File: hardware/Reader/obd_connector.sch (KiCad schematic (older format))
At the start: 3 parts, among them CN1 AHDF15A-KG-TAXB

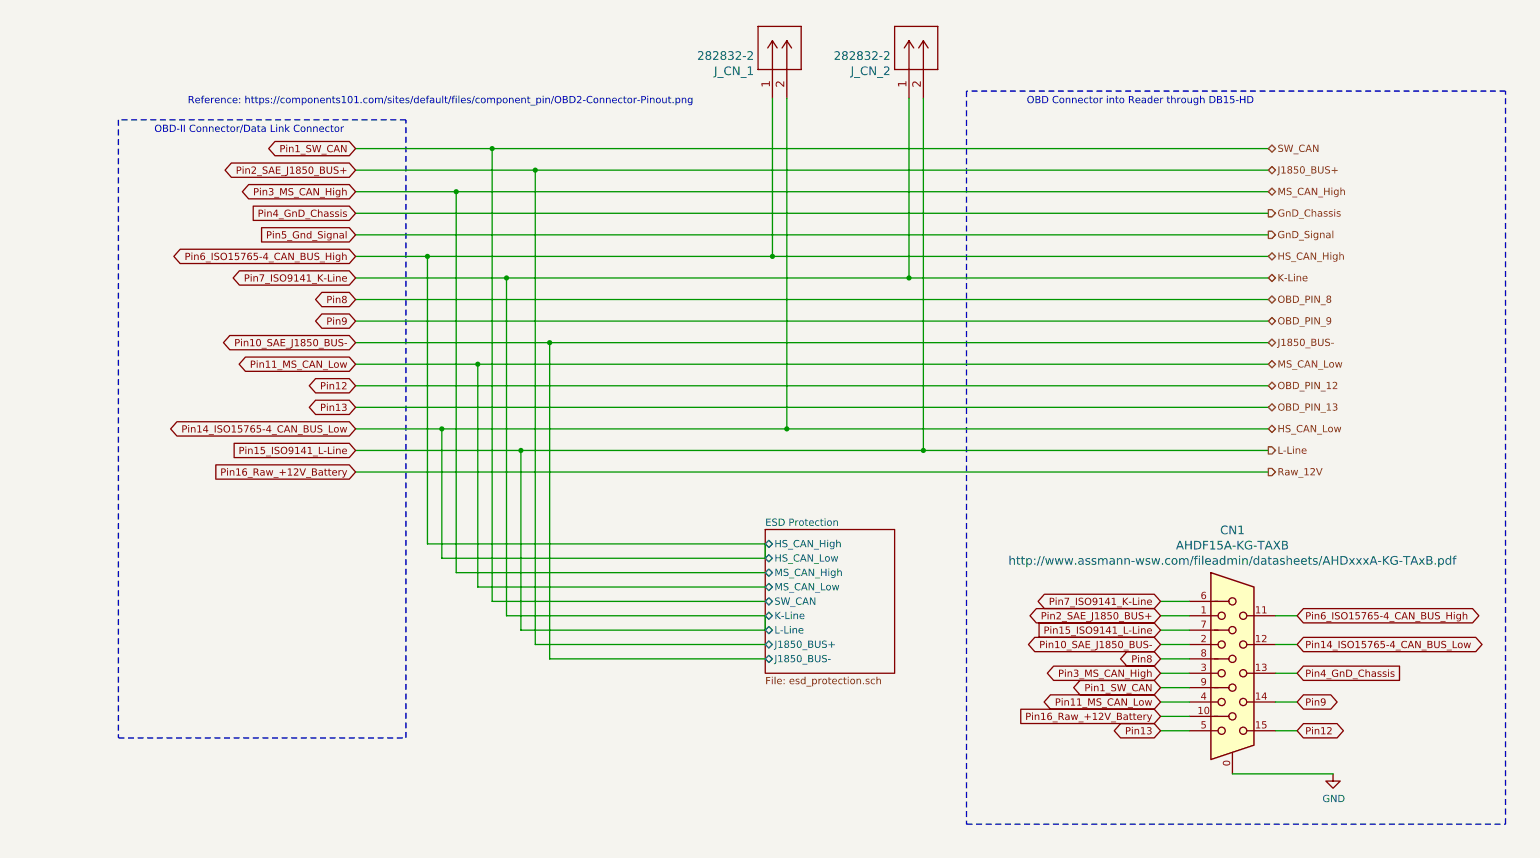
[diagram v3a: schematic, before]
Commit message: Fixed wiring issue on ESD Protection
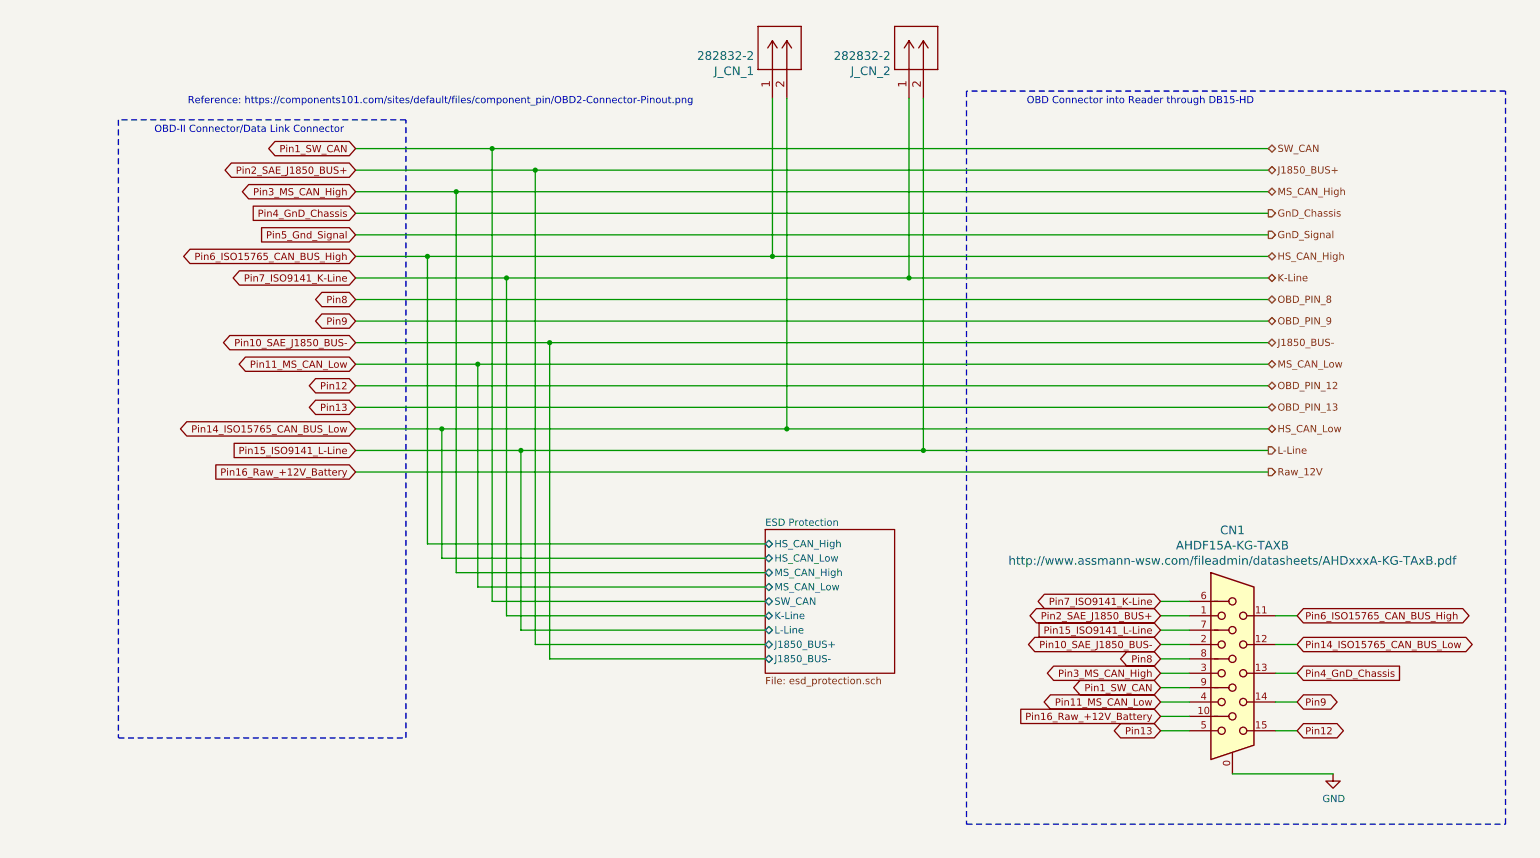
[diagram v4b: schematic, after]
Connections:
- net Pin15_ISO9141_L-Line: no longer CN1.6, J_CN_2.1
- net Pin14_ISO15765-4_CAN_BUS_Low renamed Pin14_ISO15765_CAN_BUS_Low
- net Pin14_ISO15765_CAN_BUS_Low: no longer CN1.11, J_CN_1.1
- new net Pin6_ISO15765_CAN_BUS_High: CN1.11, J_CN_1.1
- new net Pin7_ISO9141_K-Line: CN1.6, J_CN_2.1

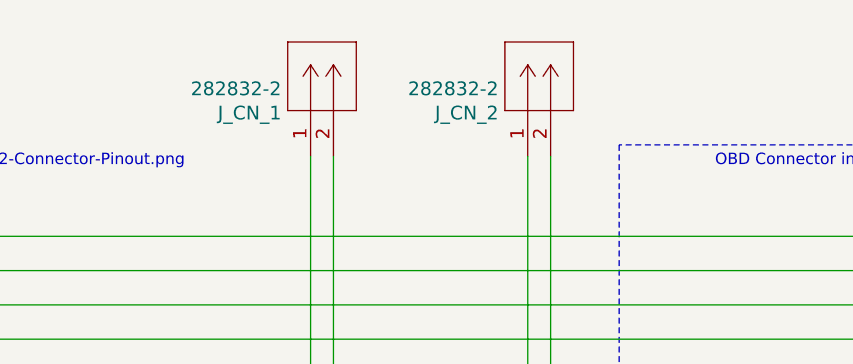
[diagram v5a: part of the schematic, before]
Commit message: Fixed bugs in schematic. Updated BOM list. Swapped to using ESP32 holder. Updated PCB layout to v0.0.2. Updated schematic to v0.0.4
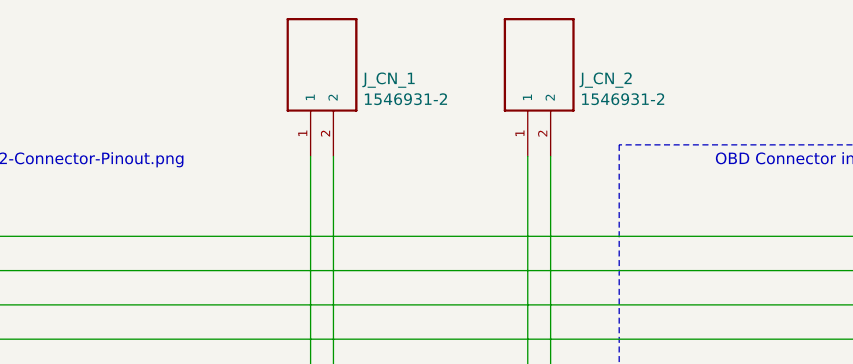
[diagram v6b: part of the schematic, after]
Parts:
- removed J_CN_1, J_CN_2: 282832-2, footprints:282832-2, symbol 2828322:282832-2
- added J_CN_1, J_CN_2: 1546931-2, footprints:1546931-2, symbol 1546931-2:1546931-2
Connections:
- net Pin14_ISO15765_CAN_BUS_Low: now also J_CN_1.2
- net Pin15_ISO9141_L-Line: now also J_CN_2.2
- net Pin6_ISO15765_CAN_BUS_High: now also J_CN_1.1
- net Pin7_ISO9141_K-Line: now also J_CN_2.1
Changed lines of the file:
@@
 Sheet 11 19
 Title "CANnect Reader | OBD Connector"
-Date "2020-10-27"
-Rev "0.0.03"
+Date "2020-10-28"
+Rev "0.0.04"
 Comp "CANtech"
 Comment1 "Created by Choong Jin Ng | jin8383@gmail.com"
@@
 	5150 2300 8600 2300
 Wire Wire Line
-	6200 1200 6200 3650
-Connection ~ 6200 3650
-Wire Wire Line
-	6200 3650 8600 3650
-Wire Wire Line
 	2750 2300 2750 4300
 Wire Wire Line
@@
 Wire Wire Line
 	3600 2900 8600 2900
-Wire Wire Line
-	3400 3650 6200 3650
 Wire Notes Line
 	10250 6250 10250 1150
@@
 Text GLabel 7850 4700 0    50   BiDi ~ 0
 Pin7_ISO9141_K-Line
-$Comp
-L 2828322:282832-2 J_CN_2
-U 1 1 5F984F05
-P 6100 1200
-F 0 "J_CN_2" V 6289 1328 60  0000 L CNN
-F 1 "282832-2" V 6395 1328 60  0000 L CNN
-F 2 "footprints:282832-2" H 6500 1140 60  0001 C CNN
-F 3 "https://www.te.com/commerce/DocumentDelivery/DDEController?Action=srchrtrv&DocNm=282832&DocType=Customer+Drawing&DocLang=English" V 6395 1328 60  0001 L CNN
-F 4 "282832-2" H 6100 1200 50  0001 C CNN "Part Name"
-F 5 "DigiKey Canada" H 6100 1200 50  0001 C CNN "Vendor"
-F 6 "TE Connectivity AMP Connectors" H 6100 1200 50  0001 C CNN "Manufacturer"
-F 7 "A113314-ND" H 6100 1200 50  0001 C CNN "digikeypn"
-	1    6100 1200
-	0    -1   -1   0
-$EndComp
 Wire Wire Line
 	5150 1200 5150 2300
-Wire Wire Line
-	3300 2450 6100 2450
-Wire Wire Line
-	6100 2450 8600 2450
-Connection ~ 6100 2450
-Wire Wire Line
-	6100 1200 6100 2450
 Wire Wire Line
 	2850 3500 5250 3500
@@
 Wire Wire Line
 	5250 1200 5250 3500
-$Comp
-L 2828322:282832-2 J_CN_1
-U 1 1 5F9847E5
-P 5150 1200
-F 0 "J_CN_1" V 5339 1328 60  0000 L CNN
-F 1 "282832-2" V 5445 1328 60  0000 L CNN
-F 2 "footprints:282832-2" H 5550 1140 60  0001 C CNN
-F 3 "https://www.te.com/commerce/DocumentDelivery/DDEController?Action=srchrtrv&DocNm=282832&DocType=Customer+Drawing&DocLang=English" V 5445 1328 60  0001 L CNN
-F 4 "282832-2" H 5150 1200 50  0001 C CNN "Part Name"
-F 5 "DigiKey Canada" H 5150 1200 50  0001 C CNN "Vendor"
-F 6 "TE Connectivity AMP Connectors" H 5150 1200 50  0001 C CNN "Manufacturer"
-F 7 "A113314-ND" H 5150 1200 50  0001 C CNN "digikeypn"
-	1    5150 1200
-	0    -1   -1   0
-$EndComp
 Wire Wire Line
 	2750 4300 5100 4300
@@
 F10 "J1850_BUS-" B L 5100 5100 50
 $EndSheet
+$Comp
+L 1546931-2:1546931-2 J_CN_1
+U 1 1 5FA0571B
+P 5250 800
+F 0 "J_CN_1" V 5189 670 50  0000 R CNN
+F 1 "1546931-2" V 5098 670 50  0000 R CNN
+F 2 "footprints:1546931-2" H 5250 800 50  0001 L BNN
+F 3 "https://www.te.com/commerce/DocumentDelivery/DDEController?Action=srchrtrv&DocNm=1-1773458-1_EURO_STYLE_QRG&DocType=DS&DocLang=English" H 5250 800 50  0001 L BNN
+F 4 "1546931-2" H 5250 800 50  0001 C CNN "Part Name"
+F 5 "TE Connectivity AMP Connectors" H 5250 800 50  0001 C CNN "Manufacturer"
+F 6 "Digikey Canada" H 5250 800 50  0001 C CNN "Vendor"
+F 7 "A97965-ND" H 5250 800 50  0001 C CNN "digikeypn"
+	1    5250 800
+	0    -1   -1   0
+$EndComp
+Connection ~ 6100 2450
+Wire Wire Line
+	6100 2450 8600 2450
+Wire Wire Line
+	3300 2450 6100 2450
+Wire Wire Line
+	3400 3650 6200 3650
+Wire Wire Line
+	6200 3650 8600 3650
+Connection ~ 6200 3650
+Wire Wire Line
+	6100 1200 6100 2450
+Wire Wire Line
+	6200 1200 6200 3650
+$Comp
+L 1546931-2:1546931-2 J_CN_2
+U 1 1 5FA083B3
+P 6200 800
+F 0 "J_CN_2" V 6139 670 50  0000 R CNN
+F 1 "1546931-2" V 6048 670 50  0000 R CNN
+F 2 "footprints:1546931-2" H 6200 800 50  0001 L BNN
+F 3 "https://www.te.com/commerce/DocumentDelivery/DDEController?Action=srchrtrv&DocNm=1-1773458-1_EURO_STYLE_QRG&DocType=DS&DocLang=English" H 6200 800 50  0001 L BNN
+F 4 "1546931-2" H 6200 800 50  0001 C CNN "Part Name"
+F 5 "TE Connectivity AMP Connectors" H 6200 800 50  0001 C CNN "Manufacturer"
+F 6 "Digikey Canada" H 6200 800 50  0001 C CNN "Vendor"
+F 7 "A97965-ND" H 6200 800 50  0001 C CNN "digikeypn"
+	1    6200 800
+	0    -1   -1   0
+$EndComp
 $EndSCHEMATC

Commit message: Revising reader
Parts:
- removed J_CN_1, J_CN_2: 1546931-2, footprints:1546931-2, symbol 1546931-2:1546931-2
- added J_CN_1: 4157, Connector_PinSocket_2.54mm:PinSocket_1x20_P2.54mm_Vertical, symbol CANtech:4157
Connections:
- net Pin10_SAE_J1850_BUS-: now also J_CN_1.12 (Pin_12)
- net Pin11_MS_CAN_Low: now also J_CN_1.17 (Pin_17)
- net Pin12: now also J_CN_1.10 (Pin_10)
- net Pin13: now also J_CN_1.11 (Pin_11)
- net Pin14_ISO15765_CAN_BUS_Low: now also J_CN_1.19 (Pin_19)
- net Pin15_ISO9141_L-Line: now also J_CN_1.14 (Pin_14)
- net Pin16_Raw_+12V_Battery: now also J_CN_1.9 (Pin_9)
- net Pin1_SW_CAN: now also J_CN_1.16 (Pin_16)
- net Pin2_SAE_J1850_BUS+: now also J_CN_1.13 (Pin_13)
- net Pin3_MS_CAN_High: now also J_CN_1.18 (Pin_18)
- net Pin4_GnD_Chassis: now also J_CN_1.5 (Pin_5)
- net Pin5_Gnd_Signal: now also J_CN_1.6 (Pin_6)
- net Pin6_ISO15765_CAN_BUS_High: now also J_CN_1.20 (Pin_20)
- net Pin7_ISO9141_K-Line: now also J_CN_1.15 (Pin_15)
- net Pin8: now also J_CN_1.7 (Pin_7)
- net Pin9: now also J_CN_1.8 (Pin_8)
- no-connect marks 0 -> 4
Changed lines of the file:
@@
 Sheet 11 19
 Title "CANnect Reader | OBD Connector"
-Date "2020-10-28"
-Rev "0.0.04"
+Date "2020-11-19"
+Rev "0.0.05"
 Comp "CANtech"
 Comment1 "Created by Choong Jin Ng | jin8383@gmail.com"
@@
 Wire Notes Line
 	10250 1150 6500 1150
-Connection ~ 5150 2300
-Wire Wire Line
-	5150 2300 8600 2300
 Wire Wire Line
 	2750 2300 2750 4300
 Wire Wire Line
-	2750 2300 5150 2300
-Wire Wire Line
 	2850 3500 2850 4400
 Wire Wire Line
@@
 	2950 1850 8600 1850
 Wire Wire Line
-	3100 3050 3100 4600
-Connection ~ 3100 3050
-Wire Wire Line
-	3100 3050 8600 3050
-Wire Wire Line
-	3200 4700 3200 1550
-Wire Wire Line
-	3200 1550 8600 1550
-Wire Wire Line
-	3300 4800 3300 2450
-Wire Wire Line
-	3400 4900 3400 3650
-Wire Wire Line
-	3500 5000 3500 1700
-Wire Wire Line
-	3500 1700 8600 1700
-Wire Wire Line
-	3600 2900 3600 5100
-Wire Wire Line
-	3600 2900 8600 2900
+	3250 4800 3250 2450
 Wire Notes Line
 	10250 6250 10250 1150
-Wire Wire Line
-	2250 3050 3100 3050
 Connection ~ 2850 3500
-Connection ~ 3400 3650
-Connection ~ 3600 2900
-Connection ~ 3300 2450
 Connection ~ 2750 2300
 Connection ~ 2950 1850
-Connection ~ 3500 1700
-Connection ~ 3200 1550
-Wire Wire Line
-	2250 3200 8600 3200
-Wire Wire Line
-	2250 2900 3600 2900
-Wire Wire Line
-	2250 2750 8600 2750
-Wire Wire Line
-	2250 2000 8600 2000
+Wire Wire Line
+	2250 2900 3550 2900
+Wire Wire Line
+	2250 2000 4250 2000
 Wire Wire Line
 	2250 1850 2950 1850
-Wire Wire Line
-	2250 1700 3500 1700
-Wire Wire Line
-	2250 1550 3200 1550
 Text GLabel 2250 2600 0    50   BiDi ~ 0
 Pin8
@@
 Pin9
 Wire Wire Line
-	2250 2150 8600 2150
+	2250 2150 4150 2150
 Wire Wire Line
 	2250 2300 2750 2300
 Wire Wire Line
-	2250 2600 8600 2600
-Wire Wire Line
-	2250 2450 3300 2450
-Wire Wire Line
-	2250 3350 8600 3350
+	2250 2600 4050 2600
+Wire Wire Line
+	2250 2450 3250 2450
+Wire Wire Line
+	2250 3350 3650 3350
 Wire Wire Line
 	2250 3500 2850 3500
-Wire Wire Line
-	2250 3800 8600 3800
-Wire Wire Line
-	2250 3650 3400 3650
 Text GLabel 2250 3650 0    50   Input ~ 0
 Pin15_ISO9141_L-Line
@@
 Pin7_ISO9141_K-Line
 Wire Wire Line
-	5150 1200 5150 2300
-Wire Wire Line
-	2850 3500 5250 3500
-Wire Wire Line
-	5250 3500 8600 3500
-Connection ~ 5250 3500
-Wire Wire Line
-	5250 1200 5250 3500
-Wire Wire Line
 	2750 4300 5100 4300
 Wire Wire Line
@@
 Wire Wire Line
 	2950 4500 5100 4500
-Wire Wire Line
-	3100 4600 5100 4600
-Wire Wire Line
-	5100 4700 3200 4700
-Wire Wire Line
-	5100 4800 3300 4800
-Wire Wire Line
-	5100 4900 3400 4900
-Wire Wire Line
-	5100 5000 3500 5000
-Wire Wire Line
-	3600 5100 5100 5100
 $Sheet
 S 5100 4200 900  1000
@@
 $EndSheet
 $Comp
-L 1546931-2:1546931-2 J_CN_1
-U 1 1 5FA0571B
-P 5250 800
-F 0 "J_CN_1" V 5189 670 50  0000 R CNN
-F 1 "1546931-2" V 5098 670 50  0000 R CNN
-F 2 "footprints:1546931-2" H 5250 800 50  0001 L BNN
-F 3 "https://www.te.com/commerce/DocumentDelivery/DDEController?Action=srchrtrv&DocNm=1-1773458-1_EURO_STYLE_QRG&DocType=DS&DocLang=English" H 5250 800 50  0001 L BNN
-F 4 "1546931-2" H 5250 800 50  0001 C CNN "Part Name"
-F 5 "TE Connectivity AMP Connectors" H 5250 800 50  0001 C CNN "Manufacturer"
-F 6 "Digikey Canada" H 5250 800 50  0001 C CNN "Vendor"
-F 7 "A97965-ND" H 5250 800 50  0001 C CNN "digikeypn"
-	1    5250 800
-	0    -1   -1   0
+L CANtech:4157 J_CN_1
+U 1 1 5FBE1A85
+P 4250 5850
+F 0 "J_CN_1" V 4663 5304 50  0000 C CNN
+F 1 "4157" V 4754 5304 50  0000 C CNN
+F 2 "Connector_PinSocket_2.54mm:PinSocket_1x20_P2.54mm_Vertical" H 4250 5850 50  0001 C CNN
+F 3 "https://media.digikey.com/pdf/Data%20Sheets/Adafruit%20PDFs/4157_Web.pdf" H 4250 5850 50  0001 C CNN
+F 4 "DigiKey Canada" H 4250 5850 50  0001 C CNN "Vendor"
+F 5 "Adafruit Industries LLC" H 4250 5850 50  0001 C CNN "Manufacturer"
+F 6 "1528-2929-ND" H 4250 5850 50  0001 C CNN "digikeypn"
+	1    4250 5850
+	0    1    1    0
 $EndComp
-Connection ~ 6100 2450
-Wire Wire Line
-	6100 2450 8600 2450
-Wire Wire Line
-	3300 2450 6100 2450
-Wire Wire Line
-	3400 3650 6200 3650
-Wire Wire Line
-	6200 3650 8600 3650
-Connection ~ 6200 3650
-Wire Wire Line
-	6100 1200 6100 2450
-Wire Wire Line
-	6200 1200 6200 3650
-$Comp
-L 1546931-2:1546931-2 J_CN_2
-U 1 1 5FA083B3
-P 6200 800
-F 0 "J_CN_2" V 6139 670 50  0000 R CNN
-F 1 "1546931-2" V 6048 670 50  0000 R CNN
-F 2 "footprints:1546931-2" H 6200 800 50  0001 L BNN
-F 3 "https://www.te.com/commerce/DocumentDelivery/DDEController?Action=srchrtrv&DocNm=1-1773458-1_EURO_STYLE_QRG&DocType=DS&DocLang=English" H 6200 800 50  0001 L BNN
-F 4 "1546931-2" H 6200 800 50  0001 C CNN "Part Name"
-F 5 "TE Connectivity AMP Connectors" H 6200 800 50  0001 C CNN "Manufacturer"
-F 6 "Digikey Canada" H 6200 800 50  0001 C CNN "Vendor"
-F 7 "A97965-ND" H 6200 800 50  0001 C CNN "digikeypn"
-	1    6200 800
-	0    -1   -1   0
-$EndComp
+Wire Wire Line
+	2750 2300 8600 2300
+Wire Wire Line
+	2850 3500 8600 3500
+Wire Wire Line
+	2750 4300 2750 5700
+Connection ~ 2750 4300
+Wire Wire Line
+	2850 5700 2850 4400
+Connection ~ 2850 4400
+Wire Wire Line
+	2950 4500 2950 5700
+Connection ~ 2950 4500
+Wire Wire Line
+	2250 3050 3050 3050
+Wire Wire Line
+	3050 3050 3050 4600
+Connection ~ 3050 3050
+Wire Wire Line
+	3050 3050 8600 3050
+Wire Wire Line
+	3050 4600 5100 4600
+Connection ~ 3050 4600
+Wire Wire Line
+	3050 4600 3050 5700
+Wire Wire Line
+	2250 1550 3150 1550
+Connection ~ 3150 1550
+Wire Wire Line
+	3150 1550 8600 1550
+Wire Wire Line
+	3150 1550 3150 4700
+Wire Wire Line
+	3150 4700 5100 4700
+Connection ~ 3150 4700
+Wire Wire Line
+	3150 4700 3150 5700
+Connection ~ 3250 2450
+Wire Wire Line
+	3250 2450 8600 2450
+Wire Wire Line
+	3250 4800 5100 4800
+Wire Wire Line
+	3250 4800 3250 5700
+Connection ~ 3250 4800
+Wire Wire Line
+	2250 3650 3350 3650
+Wire Wire Line
+	3350 5700 3350 4900
+Connection ~ 3350 3650
+Wire Wire Line
+	3350 3650 8600 3650
+Wire Wire Line
+	3350 4900 5100 4900
+Connection ~ 3350 4900
+Wire Wire Line
+	3350 4900 3350 3650
+Wire Wire Line
+	2250 1700 3450 1700
+Wire Wire Line
+	3450 1700 3450 5000
+Connection ~ 3450 1700
+Wire Wire Line
+	3450 1700 8600 1700
+Wire Wire Line
+	3450 5000 5100 5000
+Connection ~ 3450 5000
+Wire Wire Line
+	3450 5000 3450 5700
+Connection ~ 3550 2900
+Wire Wire Line
+	3550 2900 8600 2900
+Wire Wire Line
+	3550 2900 3550 5100
+Wire Wire Line
+	3550 5100 5100 5100
+Connection ~ 3550 5100
+Wire Wire Line
+	3550 5100 3550 5700
+Wire Wire Line
+	3650 5700 3650 3350
+Connection ~ 3650 3350
+Wire Wire Line
+	3650 3350 8600 3350
+Wire Wire Line
+	2250 2750 3950 2750
+Wire Wire Line
+	2250 3200 3750 3200
+Wire Wire Line
+	2250 3800 3850 3800
+Wire Wire Line
+	3750 5700 3750 3200
+Connection ~ 3750 3200
+Wire Wire Line
+	3750 3200 8600 3200
+Wire Wire Line
+	3850 5700 3850 3800
+Connection ~ 3850 3800
+Wire Wire Line
+	3850 3800 8600 3800
+Wire Wire Line
+	3950 5700 3950 2750
+Connection ~ 3950 2750
+Wire Wire Line
+	3950 2750 8600 2750
+Wire Wire Line
+	4050 5700 4050 2600
+Connection ~ 4050 2600
+Wire Wire Line
+	4050 2600 8600 2600
+Wire Wire Line
+	4150 5700 4150 2150
+Connection ~ 4150 2150
+Wire Wire Line
+	4150 2150 8600 2150
+Wire Wire Line
+	4250 2000 4250 5700
+Connection ~ 4250 2000
+Wire Wire Line
+	4250 2000 8600 2000
+NoConn ~ 4350 5700
+NoConn ~ 4450 5700
+NoConn ~ 4550 5700
+NoConn ~ 4650 5700
 $EndSCHEMATC

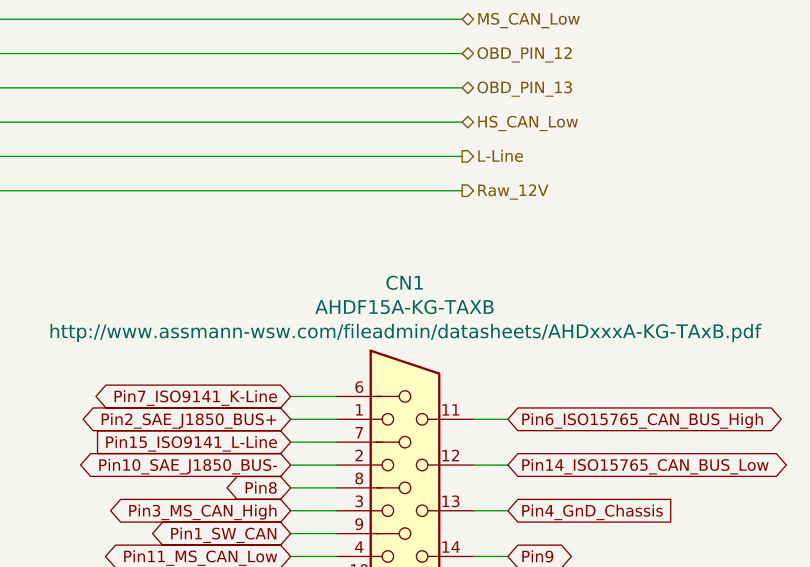
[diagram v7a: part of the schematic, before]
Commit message: Fixed numerous bugs in design for Reader Schematic and PCB
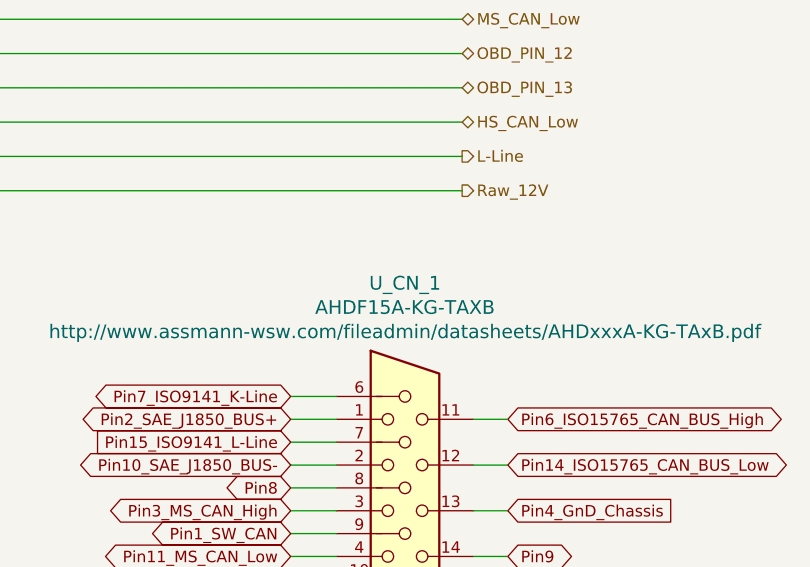
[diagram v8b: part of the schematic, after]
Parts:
- J_CN_1: Part Name (none) -> 4157
- renumbered CN1 to U_CN_1
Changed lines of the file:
@@
 P 8000 4650
 AR Path="/5FF7CC92" Ref="CN?"  Part="1"
-AR Path="/5FF6FE24/5FF7CC92" Ref="CN1"  Part="1"
-F 0 "CN1" H 8350 5095 60  0000 C CNN
+AR Path="/5FF6FE24/5FF7CC92" Ref="U_CN_1"  Part="1"
+F 0 "U_CN_1" H 8350 5095 60  0000 C CNN
 F 1 "AHDF15A-KG-TAXB" H 8350 4989 60  0000 C CNN
 F 2 "footprints:AHDF15A-KG-TAXB" H 8400 3890 60  0001 C CNN
@@
 F 5 "Adafruit Industries LLC" H 4250 5850 50  0001 C CNN "Manufacturer"
 F 6 "1528-2929-ND" H 4250 5850 50  0001 C CNN "digikeypn"
+F 7 "4157" H 4250 5850 50  0001 C CNN "Part Name"
 	1    4250 5850
 	0    1    1    0
